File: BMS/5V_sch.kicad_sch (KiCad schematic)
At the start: 15 parts, among them IC2 TPS563200DDCR

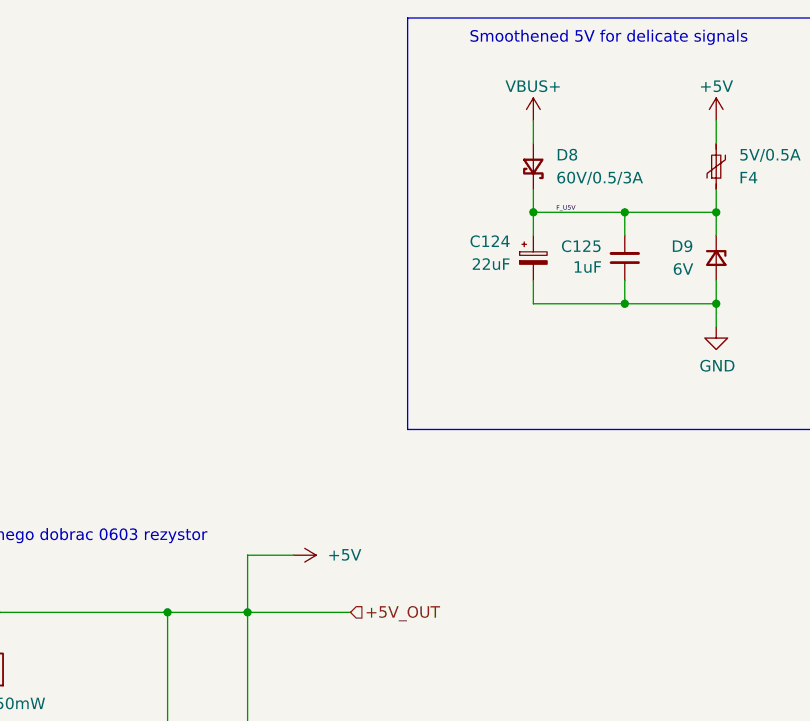
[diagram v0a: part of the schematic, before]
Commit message: Dodano layout drugiego bq79614, ukladu tlumaczącego z protokułu TI na UART oraz wstępnie poprowadzono pary różnicowe
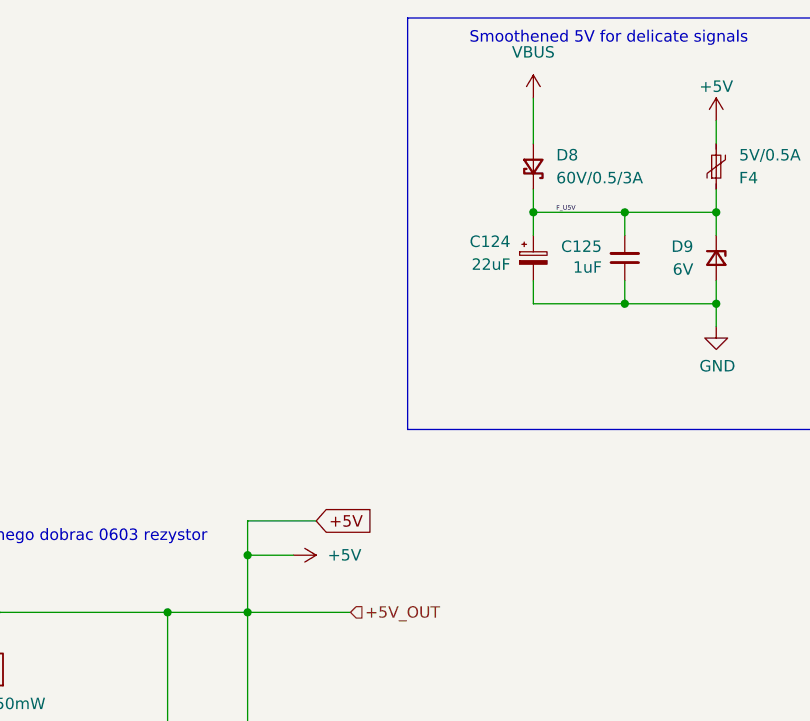
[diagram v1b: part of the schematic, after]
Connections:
- net +5V_OUT is gone; now on net +5V: C122.1, C123.1, L1.2, R165.2
- net VBUS: now reaches D8.2 (A)
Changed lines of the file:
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@@
+	)
+	(junction
+		(at 219.71 76.2)
+		(diameter 0)
+		(color 0 0 0 0)
 	)
 	(junction
@@
 	(wire
 		(pts
-			(xy 251.46 27.94) (xy 251.46 30.48)
-		)
-		(stroke
-			(width 0)
-			(type default)
-		)
-	)
-	(wire
-		(pts
 			(xy 106.68 105.41) (xy 106.68 127)
 		)
@@
 	(wire
 		(pts
+			(xy 219.71 72.39) (xy 219.71 76.2)
+		)
+		(stroke
+			(width 0)
+			(type default)
+		)
+	)
+	(wire
+		(pts
 			(xy 191.77 82.55) (xy 176.53 82.55)
 		)
@@
 	(wire
 		(pts
+			(xy 251.46 25.4) (xy 251.46 30.48)
+		)
+		(stroke
+			(width 0)
+			(type default)
+		)
+	)
+	(wire
+		(pts
 			(xy 219.71 101.6) (xy 219.71 127)
 		)
@@
 		(pts
 			(xy 271.78 48.26) (xy 271.78 50.8)
+		)
+		(stroke
+			(width 0)
+			(type default)
+		)
+	)
+	(wire
+		(pts
+			(xy 227.33 72.39) (xy 219.71 72.39)
 		)
 		(stroke
@@
 			)
 			(justify left bottom)
+		)
+	)
+	(global_label "+5V"
+		(shape input)
+		(at 227.33 72.39 0)
+		(fields_autoplaced yes)
+		(effects
+			(font
+				(size 1.27 1.27)
+			)
+			(justify left)
+		)
+		(property "Intersheetrefs" "${INTERSHEET_REFS}"
+			(at 234.1857 72.39 0)
+			(effects
+				(font
+					(size 1.27 1.27)
+				)
+				(justify left)
+				(hide yes)
+			)
 		)
 	)
@@
 	)
 	(symbol
+		(lib_id "power:VBUS")
+		(at 251.46 25.4 0)
+		(unit 1)
+		(exclude_from_sim no)
+		(in_bom yes)
+		(on_board yes)
+		(dnp no)
+		(fields_autoplaced yes)
+		(property "Reference" "#PWR034"
+			(at 251.46 29.21 0)
+			(effects
+				(font
+					(size 1.27 1.27)
+				)
+				(hide yes)
+			)
+		)
+		(property "Value" "VBUS"
+			(at 251.46 20.32 0)
+			(effects
+				(font
+					(size 1.27 1.27)
+				)
+			)
+		)
+		(property "Footprint" ""
+			(at 251.46 25.4 0)
+			(effects
+				(font
+					(size 1.27 1.27)
+				)
+				(hide yes)
+			)
+		)
+		(property "Datasheet" ""
+			(at 251.46 25.4 0)
+			(effects
+				(font
+					(size 1.27 1.27)
+				)
+				(hide yes)
+			)
+		)
+		(property "Description" "Power symbol creates a global label with name \"VBUS\""
+			(at 251.46 25.4 0)
+			(effects
+				(font
+					(size 1.27 1.27)
+				)
+				(hide yes)
+			)
+		)
+		(pin "1"
+		)
+		(instances
+			(project "BMS"
+				(path "/26289bb6-56bc-4ca1-b1a2-18d58d1afdf5/b306fb08-ef5e-4bf5-8efa-c4e5200f566a/3120d456-738f-4dcb-b831-006287d4ee74"
+					(reference "#PWR034")
+					(unit 1)
+				)
+			)
+		)
+	)
+	(symbol
 		(lib_id "Device:C_Small")
 		(at 261.62 43.18 180)
@@
 					(unit 1)
 				)
-			)
-		)
-	)
-	(symbol
-		(lib_id "power:+3.3V")
-		(at 251.46 27.94 0)
-		(unit 1)
-		(exclude_from_sim no)
-		(in_bom yes)
-		(on_board yes)
-		(dnp no)
-		(property "Reference" "#PWR0126"
-			(at 242.824 29.464 0)
-			(effects
-				(font
-					(size 1.27 1.27)
-				)
-				(hide yes)
-			)
-		)
-		(property "Value" "VBUS+"
-			(at 251.46 24.13 0)
-			(effects
-				(font
-					(size 1.27 1.27)
-				)
-			)
-		)
-		(property "Footprint" ""
-			(at 251.46 27.94 0)
-			(effects
-				(font
-					(size 1.27 1.27)
-				)
-				(hide yes)
-			)
-		)
-		(property "Datasheet" ""
-			(at 251.46 27.94 0)
-			(effects
-				(font
-					(size 1.27 1.27)
-				)
-				(hide yes)
-			)
-		)
-		(property "Description" ""
-			(at 251.46 27.94 0)
-			(effects
-				(font
-					(size 1.27 1.27)
-				)
-				(hide yes)
-			)
-		)
-		(pin "1"
-		)
-		(instances
-			(project "BMS"
-				(path "/26289bb6-56bc-4ca1-b1a2-18d58d1afdf5/b306fb08-ef5e-4bf5-8efa-c4e5200f566a/3120d456-738f-4dcb-b831-006287d4ee74"
-					(reference "#PWR0126")
-					(unit 1)
-				)

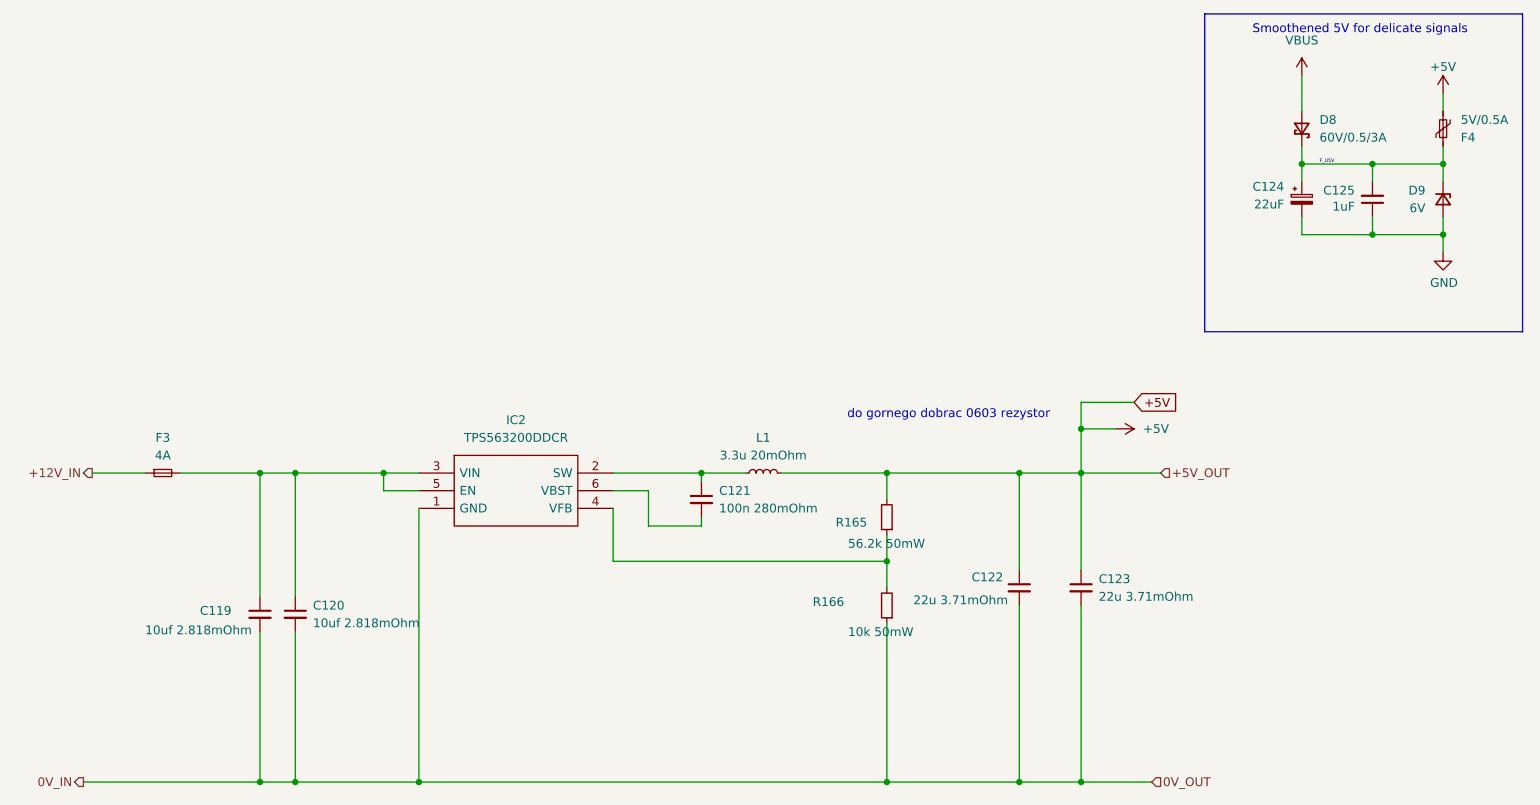
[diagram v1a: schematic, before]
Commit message: Iteracja 1.0 gotowa, teraz sprawdzenie i zmiany kosmetyczne
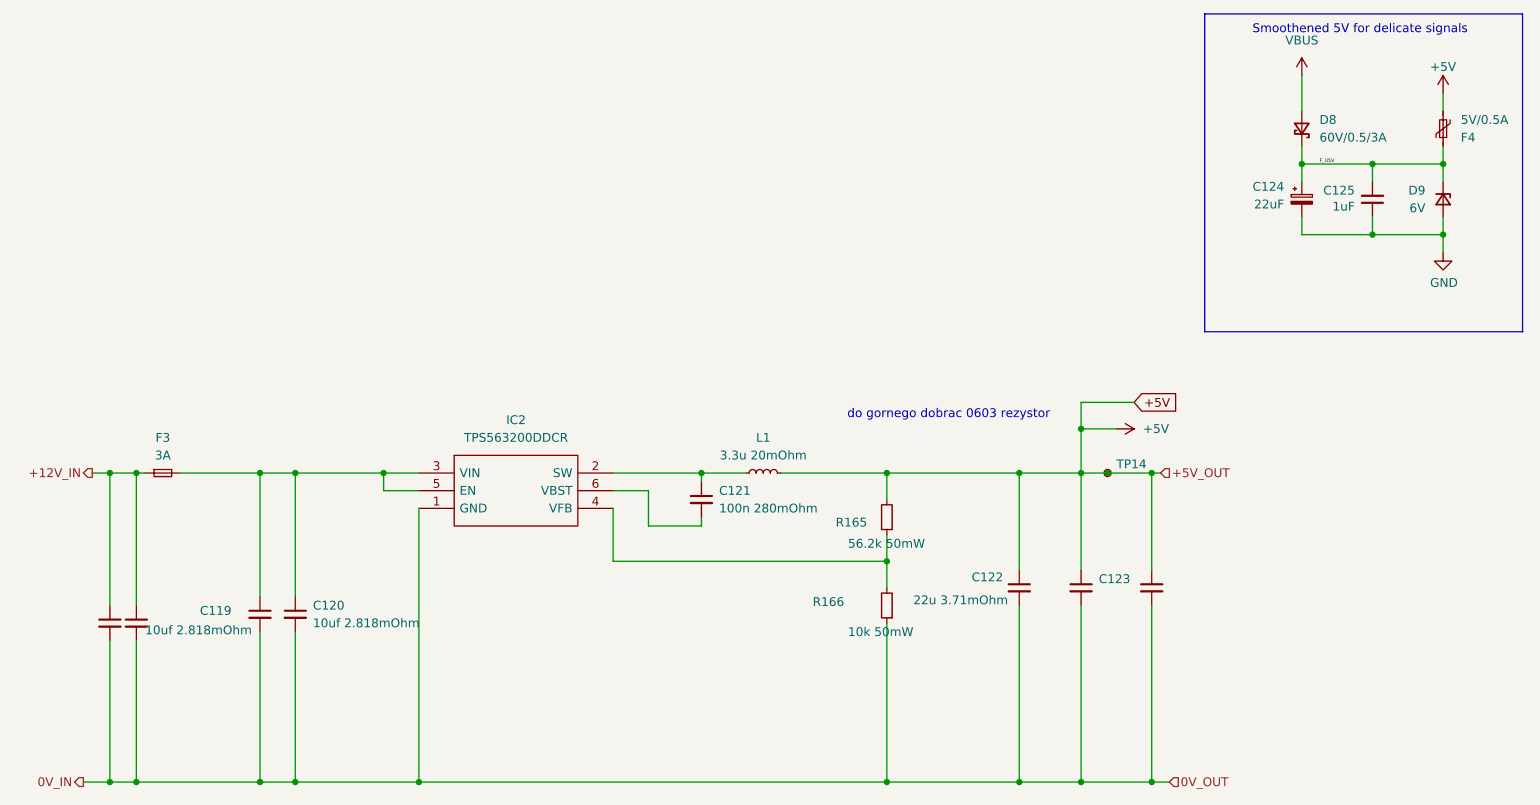
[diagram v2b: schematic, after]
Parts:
- added C134, C135, C136: 1uF, Capacitor_SMD:C_0603_1608Metric_Pad1.08x0.95mm_HandSolder, symbol Device:C_Small
- added TP14: TestPoint_Small, TestPoint:TestPoint_Pad_D1.0mm, symbol Connector:TestPoint_Small
- F3: value 4A -> 3A; footprint Resistor_SMD:R_0402_1005Metric_Pad0.72x0.64mm_HandSolder -> Fuse:Fuse_0603_1608Metric_Pad1.05x0.95mm_HandSolder
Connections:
- net +12V_IN: now also C134.1, C135.1
- net +5V: now also C136.1, TP14.1
- net 0V_IN: now also C134.2, C135.2, C136.2
